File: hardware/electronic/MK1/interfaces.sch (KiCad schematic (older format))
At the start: 4 parts

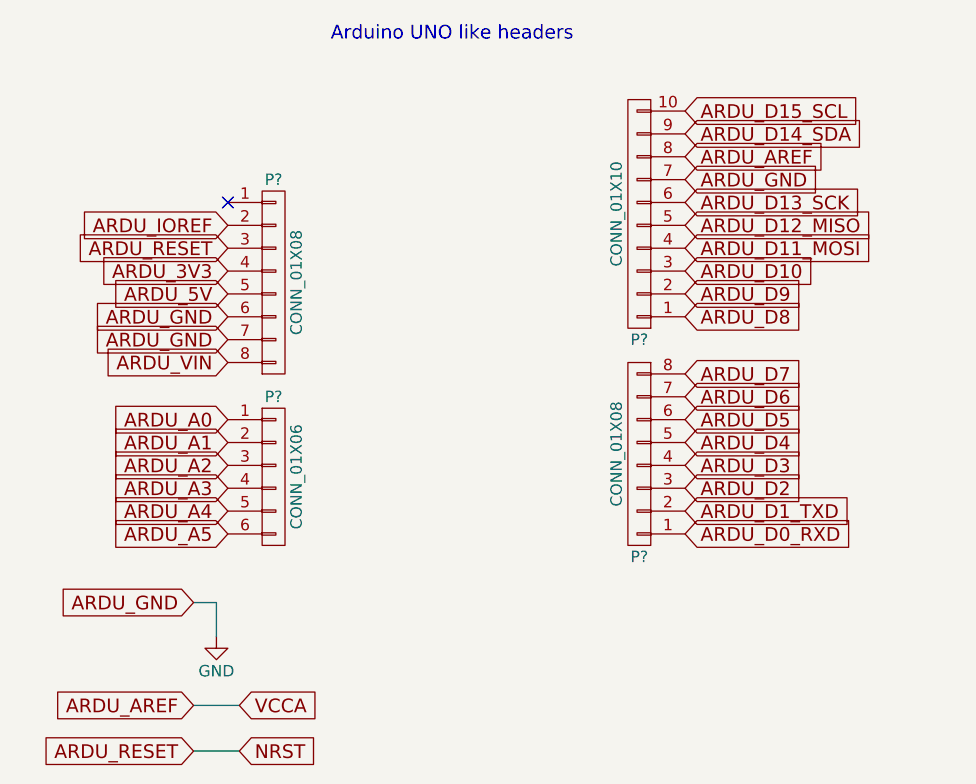
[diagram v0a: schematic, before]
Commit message: HW: First placement of MCU and headers
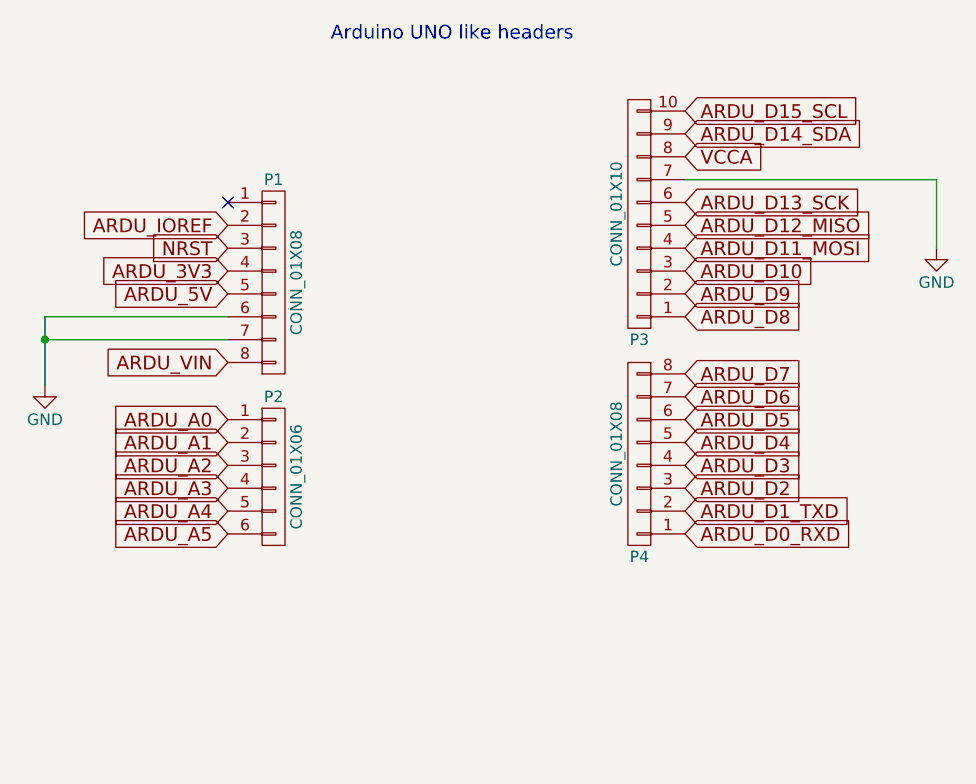
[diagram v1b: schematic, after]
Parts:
- P1, P4: renamed from P?; footprint (none) -> Socket_Strips:Socket_Strip_Straight_1x08
- P2: renamed from P?; footprint (none) -> Socket_Strips:Socket_Strip_Straight_1x06
- P3: renamed from P?; footprint (none) -> Socket_Strips:Socket_Strip_Straight_1x10
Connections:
- net ARDU_AREF renamed VCCA
- net ARDU_RESET renamed NRST
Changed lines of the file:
@@
 Arduino UNO like headers
 $Comp
-L CONN_01X10 P?
+L CONN_01X10 P3
 U 1 1 58866D50
 P 3350 1700
-F 0 "P?" H 3350 2250 50  0000 C CNN
+F 0 "P3" H 3350 2250 50  0000 C CNN
 F 1 "CONN_01X10" V 3450 1700 50  0000 C CNN
-F 2 "" H 3350 1700 50  0000 C CNN
+F 2 "Socket_Strips:Socket_Strip_Straight_1x10" H 3350 1700 50  0001 C CNN
 F 3 "" H 3350 1700 50  0000 C CNN
 	1    3350 1700
@@
 $EndComp
 $Comp
-L CONN_01X08 P?
+L CONN_01X08 P4
 U 1 1 58866E4A
 P 3350 2750
-F 0 "P?" H 3350 3200 50  0000 C CNN
+F 0 "P4" H 3350 3200 50  0000 C CNN
 F 1 "CONN_01X08" V 3450 2750 50  0000 C CNN
-F 2 "" H 3350 2750 50  0000 C CNN
+F 2 "Socket_Strips:Socket_Strip_Straight_1x08" H 3350 2750 50  0001 C CNN
 F 3 "" H 3350 2750 50  0000 C CNN
 	1    3350 2750
@@
 $EndComp
 $Comp
-L CONN_01X08 P?
+L CONN_01X08 P1
 U 1 1 58866E83
 P 1750 2000
-F 0 "P?" H 1750 2450 50  0000 C CNN
+F 0 "P1" H 1750 2450 50  0000 C CNN
 F 1 "CONN_01X08" V 1850 2000 50  0000 C CNN
-F 2 "" H 1750 2000 50  0000 C CNN
+F 2 "Socket_Strips:Socket_Strip_Straight_1x08" H 1750 2000 50  0001 C CNN
 F 3 "" H 1750 2000 50  0000 C CNN
 	1    1750 2000
@@
 $EndComp
 $Comp
-L CONN_01X06 P?
+L CONN_01X06 P2
 U 1 1 58866F7C
 P 1750 2850
-F 0 "P?" H 1750 3200 50  0000 C CNN
+F 0 "P2" H 1750 3200 50  0000 C CNN
 F 1 "CONN_01X06" V 1850 2850 50  0000 C CNN
-F 2 "" H 1750 2850 50  0000 C CNN
+F 2 "Socket_Strips:Socket_Strip_Straight_1x06" H 1750 2850 50  0001 C CNN
 F 3 "" H 1750 2850 50  0000 C CNN
 	1    1750 2850
@@
 ARDU_D14_SDA
 Text GLabel 3550 1450 2    60   Input ~ 0
-ARDU_AREF
-Text GLabel 3550 1550 2    60   Input ~ 0
-ARDU_GND
+VCCA
 Text GLabel 3550 1650 2    60   Input ~ 0
 ARDU_D13_SCK
@@
 ARDU_IOREF
 Text GLabel 1550 1850 0    60   Input ~ 0
-ARDU_RESET
+NRST
 Text GLabel 1550 1950 0    60   Input ~ 0
 ARDU_3V3
 Text GLabel 1550 2050 0    60   Input ~ 0
 ARDU_5V
-Text GLabel 1550 2150 0    60   Input ~ 0
-ARDU_GND
-Text GLabel 1550 2250 0    60   Input ~ 0
-ARDU_GND
 Text GLabel 1550 2350 0    60   Input ~ 0
 ARDU_VIN
@@
 Text GLabel 1550 3100 0    60   Input ~ 0
 ARDU_A5
-Text GLabel 1400 3400 0    60   Input ~ 0
-ARDU_GND
-Wire Wire Line
-	1400 3400 1500 3400
-Wire Wire Line
-	1500 3400 1500 3550
 $Comp
-L GND #PWR?
+L GND #PWR08
 U 1 1 5886770A
-P 1500 3550
-F 0 "#PWR?" H 1500 3300 50  0001 C CNN
-F 1 "GND" H 1500 3400 50  0000 C CNN
-F 2 "" H 1500 3550 50  0000 C CNN
-F 3 "" H 1500 3550 50  0000 C CNN
-	1    1500 3550
+P 750 2450
+F 0 "#PWR08" H 750 2200 50  0001 C CNN
+F 1 "GND" H 750 2300 50  0000 C CNN
+F 2 "" H 750 2450 50  0000 C CNN
+F 3 "" H 750 2450 50  0000 C CNN
+	1    750  2450
 	1    0    0    -1
 $EndComp
-Text GLabel 1400 3850 0    60   Input ~ 0
-ARDU_AREF
+NoConn ~ 1550 1650
 Wire Wire Line
-	1400 3850 1600 3850
-Text GLabel 1600 3850 2    60   Input ~ 0
-VCCA
-Text GLabel 1400 4050 0    60   Input ~ 0
-ARDU_RESET
+	3550 1550 4650 1550
 Wire Wire Line
-	1400 4050 1600 4050
-Text GLabel 1600 4050 2    60   Input ~ 0
-NRST
-NoConn ~ 1550 1650
+	4650 1550 4650 1850
+$Comp
+L GND #PWR09
+U 1 1 5886A835
+P 4650 1850
+F 0 "#PWR09" H 4650 1600 50  0001 C CNN
+F 1 "GND" H 4650 1700 50  0000 C CNN
+F 2 "" H 4650 1850 50  0000 C CNN
+F 3 "" H 4650 1850 50  0000 C CNN
+	1    4650 1850
+	1    0    0    -1
+$EndComp
+Wire Wire Line
+	1550 2150 750  2150
+Wire Wire Line
+	750  2150 750  2450
+Wire Wire Line
+	1550 2250 750  2250
+Connection ~ 750  2250
 $EndSCHEMATC
